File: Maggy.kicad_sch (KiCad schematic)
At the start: 75 parts, among them CN1 0430450800, CN2 430451000, J1 XY308-2.54-2P, J2 XY308-2.54-2P, J3 XY308-2.54-2P, J4 XY308-2.54-2P, U1 CH224K, U10 INA214AIDCKR, U11 Socket for Teensy 4.1 (2x 1x2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, U12 INA214AIDCKR, U13 INA214AIDCKR, U14 TMAG5170A2DGKR, U15 TMAG5170A2DGKR, U16 TMAG5170A2DGKR, U17 TMAG5170A2DGKR, U18 TMAG5170A2DGKR, U2 A4950ELJTR-T, U3 A4950ELJTR-T, U4 A4950ELJTR-T, U5 A4950ELJTR-T, U6 TLV2372, U7 LM1117S-3.3, U8 LM1117S-5.0, U9 INA214AIDCKR

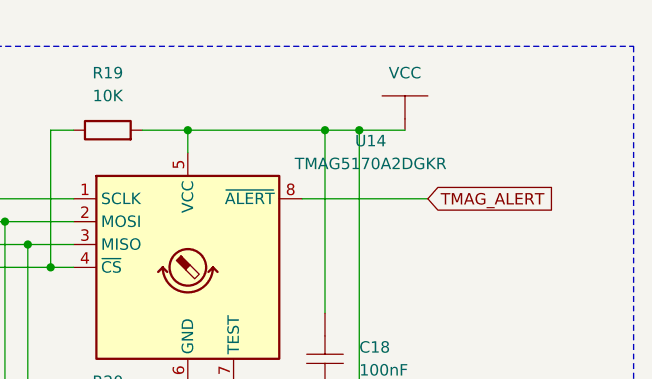
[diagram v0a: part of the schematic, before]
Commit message: fix: update SPI-sensors' power source from VCC to 3v3
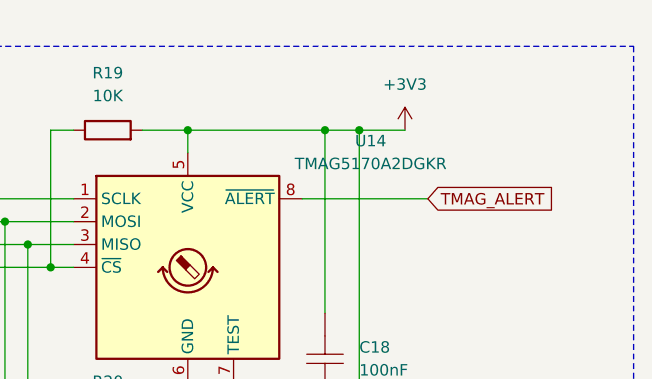
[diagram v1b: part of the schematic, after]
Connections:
- net VCC is gone; now on net +3V3: C18.2, C19.2, C20.2, C21.2, C22.2, R19.2, R20.2, R21.2, R22.2, R23.2, U14.5 (VCC), U15.5 (VCC), U16.5 (VCC), U17.5 (VCC), U18.5 (VCC)
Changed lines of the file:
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@@
 	)
 	(symbol
+		(lib_id "power:+3V3")
+		(at 397.51 31.75 0)
+		(unit 1)
+		(body_style 1)
+		(exclude_from_sim no)
+		(in_bom yes)
+		(on_board yes)
+		(in_pos_files yes)
+		(dnp no)
+		(fields_autoplaced yes)
+		(property "Reference" "#PWR056"
+			(at 397.51 35.56 0)
+			(hide yes)
+			(show_name no)
+			(do_not_autoplace no)
+			(effects
+				(font
+					(size 1.27 1.27)
+				)
+			)
+		)
+		(property "Value" "+3V3"
+			(at 397.51 26.67 0)
+			(show_name no)
+			(do_not_autoplace no)
+			(effects
+				(font
+					(size 1.27 1.27)
+				)
+			)
+		)
+		(property "Footprint" ""
+			(at 397.51 31.75 0)
+			(hide yes)
+			(show_name no)
+			(do_not_autoplace no)
+			(effects
+				(font
+					(size 1.27 1.27)
+				)
+			)
+		)
+		(property "Datasheet" ""
+			(at 397.51 31.75 0)
+			(hide yes)
+			(show_name no)
+			(do_not_autoplace no)
+			(effects
+				(font
+					(size 1.27 1.27)
+				)
+			)
+		)
+		(property "Description" "Power symbol creates a global label with name \"+3V3\""
+			(at 397.51 31.75 0)
+			(hide yes)
+			(show_name no)
+			(do_not_autoplace no)
+			(effects
+				(font
+					(size 1.27 1.27)
+				)
+			)
+		)
+		(pin "1"
+		)
+		(instances
+			(project "Maggy"
+				(path "/52283d6a-1d9f-44e8-81a2-e61315819c23"
+					(reference "#PWR056")
+					(unit 1)
+				)
+			)
+		)
+	)
+	(symbol
 		(lib_id "ProPrj_Mag-easyedapro:CAP")
 		(at 388.62 194.31 270)
@@
 					(unit 1)
 				)
-			)
-		)
-	)
-	(symbol
-		(lib_name "Power-VCC_2")
-		(lib_id "ProPrj_Mag-easyedapro:Power-VCC")
-		(at 397.51 31.75 0)
-		(unit 1)
-		(body_style 1)
-		(exclude_from_sim no)
-		(in_bom yes)
-		(on_board yes)
-		(in_pos_files yes)
-		(dnp no)
-		(fields_autoplaced yes)
-		(property "Reference" "#PWR056"
-			(at 397.51 31.75 0)
-			(hide yes)
-			(show_name no)
-			(do_not_autoplace no)
-			(effects
-				(font
-					(size 1.27 1.27)
-				)
-			)
-		)
-		(property "Value" "VCC"
-			(at 397.51 25.4 0)
-			(show_name no)
-			(do_not_autoplace no)
-			(effects
-				(font
-					(size 1.27 1.27)
-				)
-			)
-		)
-		(property "Footprint" "ProPrj_Mag-easyedapro:"
-			(at 397.51 31.75 0)
-			(hide yes)
-			(show_name no)
-			(do_not_autoplace no)
-			(effects
-				(font
-					(size 1.27 1.27)
-				)
-			)
-		)
-		(property "Datasheet" ""
-			(at 397.51 31.75 0)
-			(hide yes)
-			(show_name no)
-			(do_not_autoplace no)
-			(effects
-				(font
-					(size 1.27 1.27)
-				)
-			)
-		)
-		(property "Description" ""
-			(at 397.51 31.75 0)
-			(hide yes)
-			(show_name no)
-			(do_not_autoplace no)
-			(effects
-				(font
-					(size 1.27 1.27)
-				)
-			)
-		)
-		(pin "1"
-		)
-		(instances
-			(project "Maggy"
-				(path "/52283d6a-1d9f-44e8-81a2-e61315819c23"
-					(reference "#PWR056")
-					(unit 1)
-				)

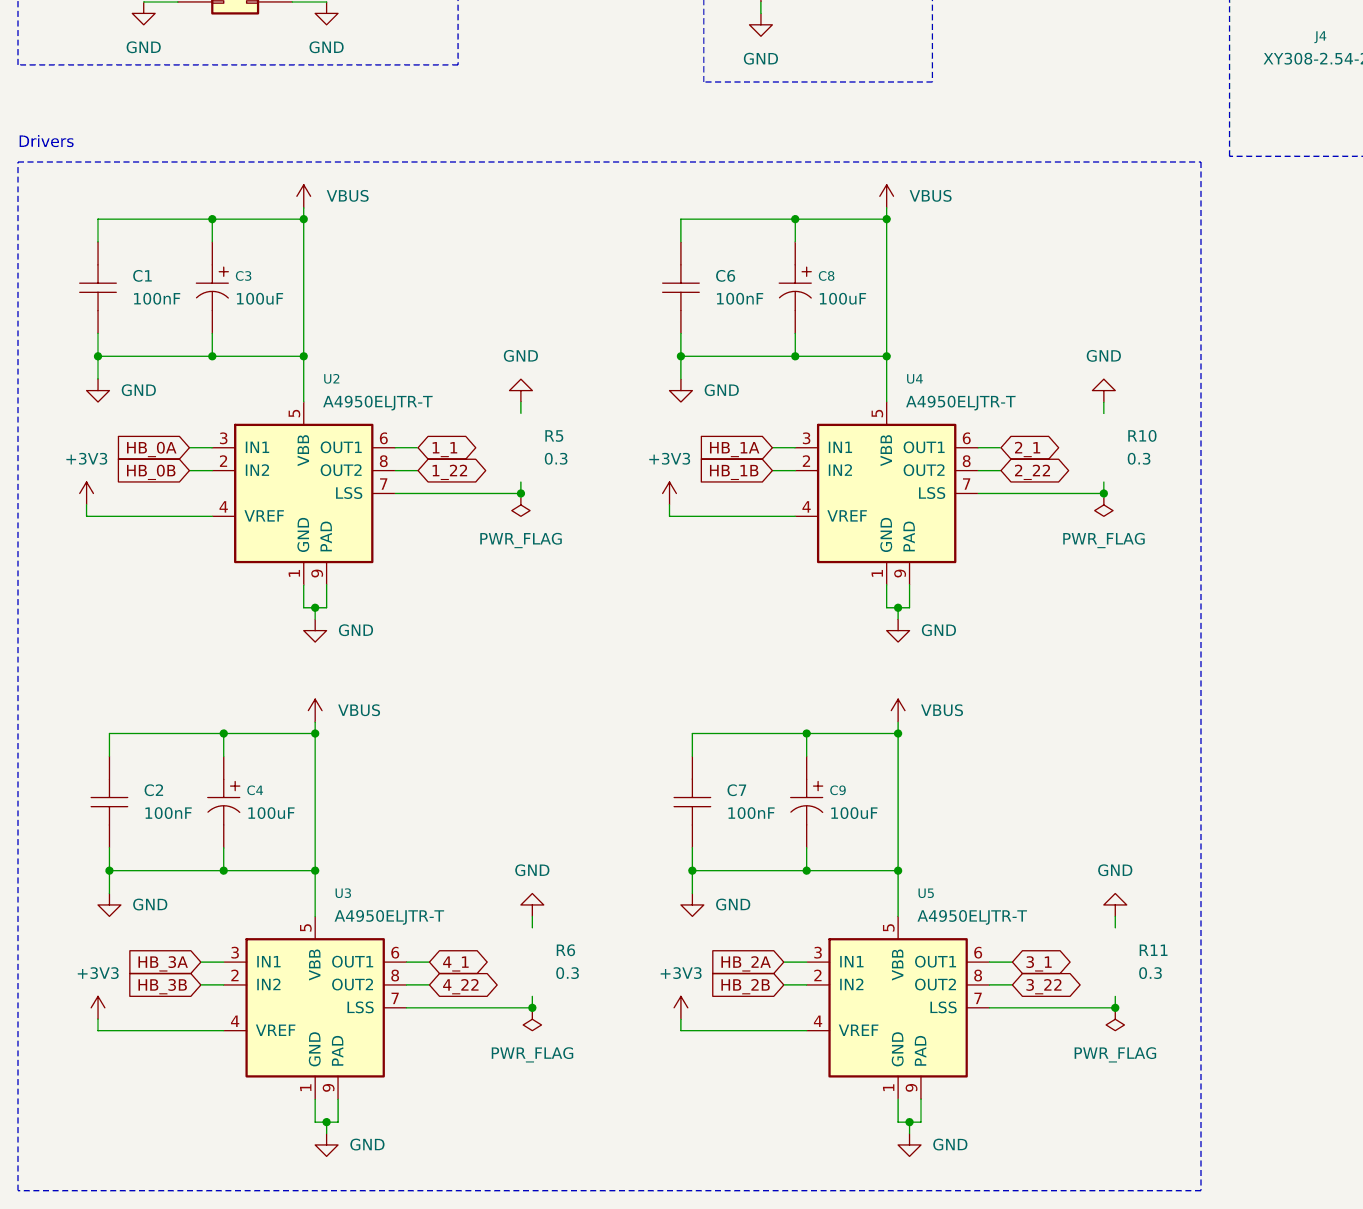
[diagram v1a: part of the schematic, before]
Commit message: fix!: resolve short between VBUS and GND near motor drivers
During the migration from EasyEDA, a mistake was introduced shorting VBUS to GND near the power supply for each motor driver. This was caught by the ERC, and this commit removes the shorted connection.
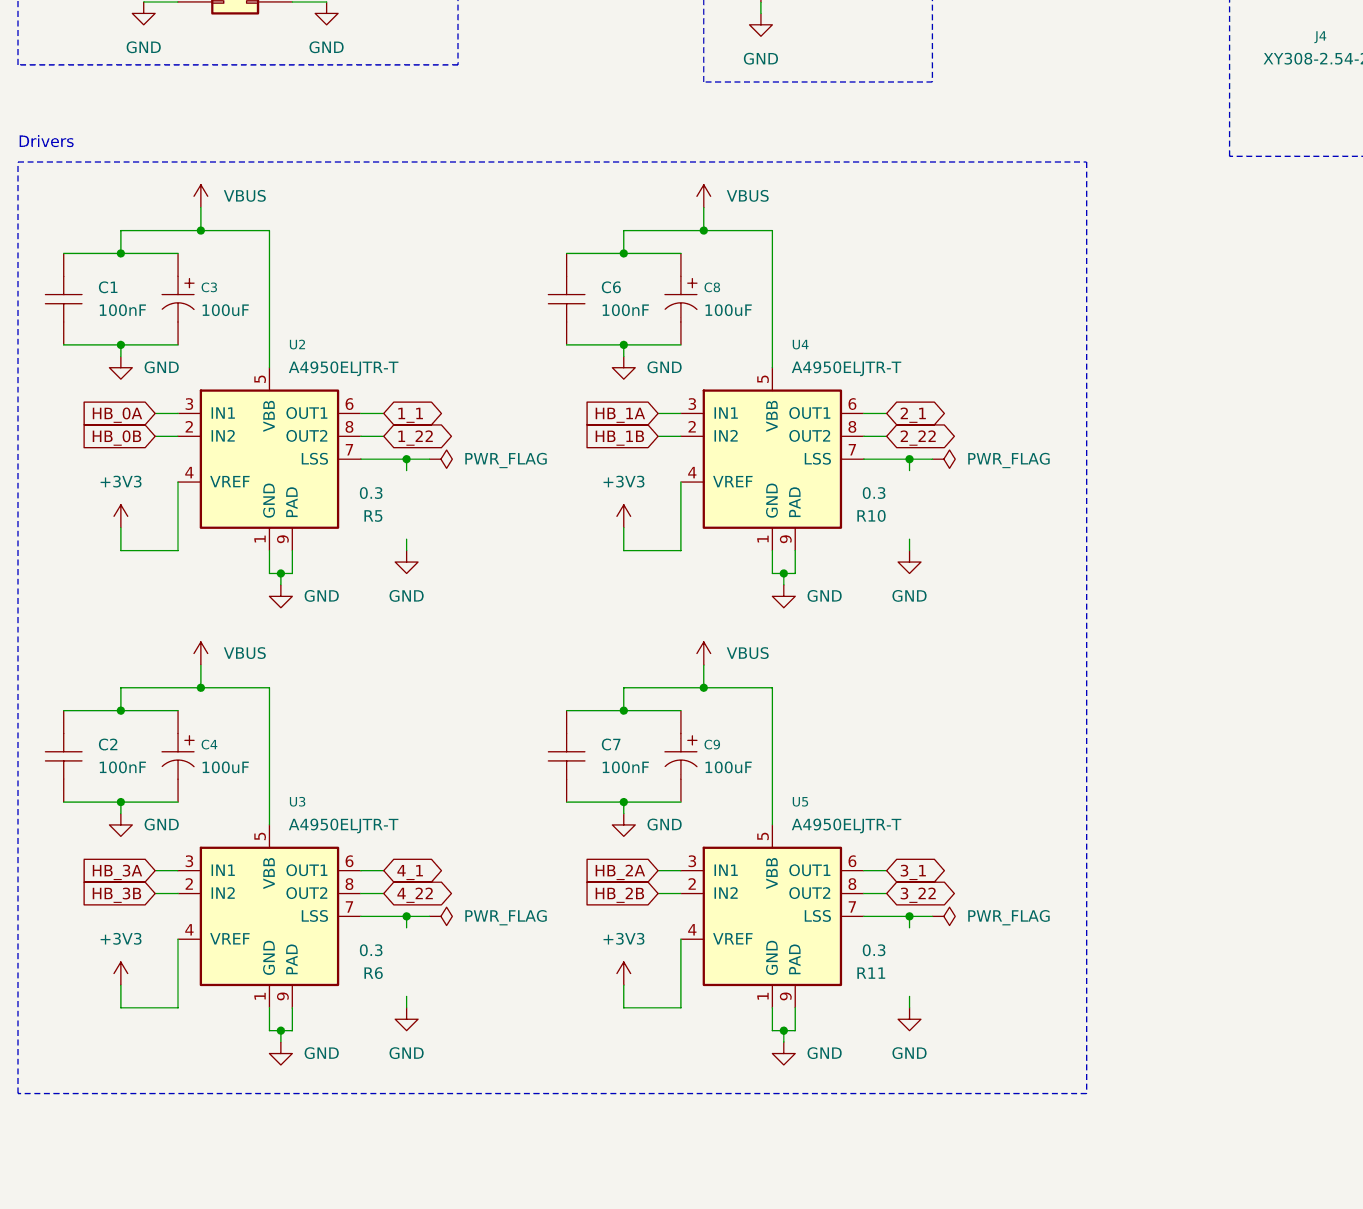
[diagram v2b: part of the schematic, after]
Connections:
- net GND: no longer C1.1, C10.1, C11.1, C2.1, C3.1, C4.1, C6.1, C7.1, C8.1, C9.1, R1.2, R2.2, R7.2, U2.5 (VBB), U3.5 (VBB), U4.5 (VBB), U5.5 (VBB), U7.3 (VI), U8.3 (VI), USBC1.A4 (VBUS), USBC1.A9 (VBUS), USBC1.B4 (VBUS), USBC1.B9 (VBUS)
- new net VBUS: C1.1, C10.1, C11.1, C2.1, C3.1, C4.1, C6.1, C7.1, C8.1, C9.1, R1.2, R2.2, R7.2, U2.5 (VBB), U3.5 (VBB), U4.5 (VBB), U5.5 (VBB), U7.3 (VI), U8.3 (VI), USBC1.A4 (VBUS), USBC1.A9 (VBUS), USBC1.B4 (VBUS), USBC1.B9 (VBUS)
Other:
- moved on the sheet: C1, C3, U2

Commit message: chore: replace all EasyEDA capacitor symbols with KiCad native ones
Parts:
- C1, C10, C11, C12, C13, C14, C15, C16, C17, C18, C19, C2, C20, C21, C22, C5, C6, C7: symbol ProPrj_Mag-easyedapro:CAP -> Device:C
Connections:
- net +3V3: now also C13.2, C14.1, C15.1, C16.1, C17.1, C18.1, C19.1, C20.1, C21.1, C22.1, C5.2; no longer C13.1, C14.2, C15.2, C16.2, C17.2, C18.2, C19.2, C20.2, C21.2, C22.2, C5.1
- net +5V: now also C12.2; no longer C12.1
- net GND: now also C1.1, C10.1, C11.1, C12.1, C13.1, C14.2, C15.2, C16.2, C17.2, C18.2, C19.2, C2.1, C20.2, C21.2, C22.2, C5.1, C6.1, C7.1; no longer C1.2, C10.2, C11.2, C12.2, C13.2, C14.1, C15.1, C16.1, C17.1, C18.1, C19.1, C2.2, C20.1, C21.1, C22.1, C5.2, C6.2, C7.2
- net VBUS: now also C1.2, C10.2, C11.2, C2.2, C6.2, C7.2; no longer C1.1, C10.1, C11.1, C2.1, C6.1, C7.1

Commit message: chore: replace all EasyEDA polarized capacitor symbols with KiCad native ones
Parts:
- C3, C4, C8, C9: symbol ProPrj_Mag-easyedapro:RST100UF35V009 -> Device:C_Polarized_US
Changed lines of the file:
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@@
 	(wire
 		(pts
+			(xy 35.56 209.55) (xy 35.56 210.82)
+		)
+		(stroke
+			(width 0)
+			(type default)
+		)
+	)
+	(wire
+		(pts
 			(xy 29.21 207.01) (xy 29.21 209.55)
 		)
@@
 	(wire
 		(pts
+			(xy 35.56 260.35) (xy 35.56 261.62)
+		)
+		(stroke
+			(width 0)
+			(type default)
+		)
+	)
+	(wire
+		(pts
 			(xy 269.24 280.67) (xy 302.26 280.67)
 		)
@@
 	(wire
 		(pts
+			(xy 91.44 209.55) (xy 91.44 210.82)
+		)
+		(stroke
+			(width 0)
+			(type default)
+		)
+	)
+	(wire
+		(pts
 			(xy 233.68 71.12) (xy 234.95 71.12)
 		)
@@
 	(wire
 		(pts
+			(xy 35.56 218.44) (xy 35.56 219.71)
+		)
+		(stroke
+			(width 0)
+			(type default)
+		)
+	)
+	(wire
+		(pts
 			(xy 88.9 278.13) (xy 91.44 278.13)
 		)
@@
 	(wire
 		(pts
+			(xy 91.44 218.44) (xy 91.44 219.71)
+		)
+		(stroke
+			(width 0)
+			(type default)
+		)
+	)
+	(wire
+		(pts
+			(xy 91.44 260.35) (xy 91.44 261.62)
+		)
+		(stroke
+			(width 0)
+			(type default)
+		)
+	)
+	(wire
+		(pts
 			(xy 396.24 165.1) (xy 396.24 199.39)
 		)
@@
 	(wire
 		(pts
+			(xy 91.44 269.24) (xy 91.44 270.51)
+		)
+		(stroke
+			(width 0)
+			(type default)
+		)
+	)
+	(wire
+		(pts
 			(xy 378.46 199.39) (xy 388.62 199.39)
 		)
@@
 	(wire
 		(pts
+			(xy 35.56 269.24) (xy 35.56 270.51)
+		)
+		(stroke
+			(width 0)
+			(type default)
+		)
+	)
+	(wire
+		(pts
 			(xy 114.3 278.13) (xy 111.76 278.13)
 		)
@@
 	)
 	(symbol
-		(lib_id "ProPrj_Mag-easyedapro:RST100UF35V009")
-		(at 35.56 214.63 270)
+		(lib_id "Device:C_Polarized_US")
+		(at 35.56 214.63 0)
 		(unit 1)
-		(body_style 0)
+		(body_style 1)
 		(exclude_from_sim no)
 		(in_bom yes)
@@
 		(fields_autoplaced yes)
 		(property "Reference" "C3"
-			(at 38.1 213.36 90)
+			(at 39.37 212.725 0)
 			(show_name no)
 			(do_not_autoplace no)
@@
 		)
 		(property "Value" "100uF"
-			(at 38.1 215.8999 90)
+			(at 39.37 215.2649 0)
 			(show_name no)
 			(do_not_autoplace no)
@@
 			)
 		)
-		(property "Description" "Capacitance: Tolerance:±20% Tolerance:±20% Rated Voltage: Ripple Current:84mA@120Hz Equivalent Series Resistance(ESR):- φD: L: Lifetime @ Temp:2000hrs@105℃ Operating Temperature:-40℃~+105℃ Operating Temperature:-40℃~+105℃"
-			(at 35.56 214.63 90)
+		(property "Description" "Polarized capacitor, US symbol"
+			(at 35.56 214.63 0)
 			(hide yes)
 			(show_name no)
@@
 					(size 1.27 1.27)
 				)
-				(justify left bottom)
 			)
 		)
@@
 	)
 	(symbol
-		(lib_id "ProPrj_Mag-easyedapro:RST100UF35V009")
-		(at 35.56 265.43 270)
+		(lib_id "Device:C_Polarized_US")
+		(at 35.56 265.43 0)
 		(unit 1)
 		(body_style 0)
@@
 		(fields_autoplaced yes)
 		(property "Reference" "C4"
-			(at 38.1 264.16 90)
+			(at 39.37 263.525 0)
 			(show_name no)
 			(do_not_autoplace no)
@@
 		)
 		(property "Value" "100uF"
-			(at 38.1 266.6999 90)
+			(at 39.37 266.0649 0)
 			(show_name no)
 			(do_not_autoplace no)
@@
 			)
 		)
-		(property "Description" "Capacitance: Tolerance:±20% Tolerance:±20% Rated Voltage: Ripple Current:84mA@120Hz Equivalent Series Resistance(ESR):- φD: L: Lifetime @ Temp:2000hrs@105℃ Operating Temperature:-40℃~+105℃ Operating Temperature:-40℃~+105℃"
-			(at 35.56 265.43 90)
+		(property "Description" "Polarized capacitor, US symbol"
+			(at 35.56 265.43 0)
 			(hide yes)
 			(show_name no)
@@
 					(size 1.27 1.27)
 				)
-				(justify left bottom)
 			)
 		)
@@
 	)
 	(symbol
-		(lib_id "ProPrj_Mag-easyedapro:RST100UF35V009")
-		(at 91.44 265.43 270)
+		(lib_id "Device:C_Polarized_US")
+		(at 91.44 265.43 0)
 		(unit 1)
 		(body_style 0)
@@
 		(fields_autoplaced yes)
 		(property "Reference" "C9"
-			(at 93.98 264.16 90)
+			(at 95.25 263.525 0)
 			(show_name no)
 			(do_not_autoplace no)
@@
 		)
 		(property "Value" "100uF"
-			(at 93.98 266.6999 90)
+			(at 95.25 266.0649 0)
 			(show_name no)
 			(do_not_autoplace no)
@@
 			)
 		)
-		(property "Description" "Capacitance: Tolerance:±20% Tolerance:±20% Rated Voltage: Ripple Current:84mA@120Hz Equivalent Series Resistance(ESR):- φD: L: Lifetime @ Temp:2000hrs@105℃ Operating Temperature:-40℃~+105℃ Operating Temperature:-40℃~+105℃"
-			(at 91.44 265.43 90)
+		(property "Description" "Polarized capacitor, US symbol"
+			(at 91.44 265.43 0)
 			(hide yes)
 			(show_name no)
@@
 					(size 1.27 1.27)
 				)
-				(justify left bottom)
 			)
 		)
@@
 	)
 	(symbol
-		(lib_id "ProPrj_Mag-easyedapro:RST100UF35V009")
-		(at 91.44 214.63 270)
+		(lib_id "Device:C_Polarized_US")
+		(at 91.44 214.63 0)
 		(unit 1)
 		(body_style 0)
@@
 		(fields_autoplaced yes)
 		(property "Reference" "C8"
-			(at 93.98 213.36 90)
+			(at 95.25 212.725 0)
 			(show_name no)
 			(do_not_autoplace no)
@@
 		)
 		(property "Value" "100uF"
-			(at 93.98 215.8999 90)
+			(at 95.25 215.2649 0)
 			(show_name no)
 			(do_not_autoplace no)
@@
 			)
 		)
-		(property "Description" "Capacitance: Tolerance:±20% Tolerance:±20% Rated Voltage: Ripple Current:84mA@120Hz Equivalent Series Resistance(ESR):- φD: L: Lifetime @ Temp:2000hrs@105℃ Operating Temperature:-40℃~+105℃ Operating Temperature:-40℃~+105℃"
-			(at 91.44 214.63 90)
+		(property "Description" "Polarized capacitor, US symbol"
+			(at 91.44 214.63 0)
 			(hide yes)
 			(show_name no)
@@
 					(size 1.27 1.27)
 				)
-				(justify left bottom)
 			)
 		)

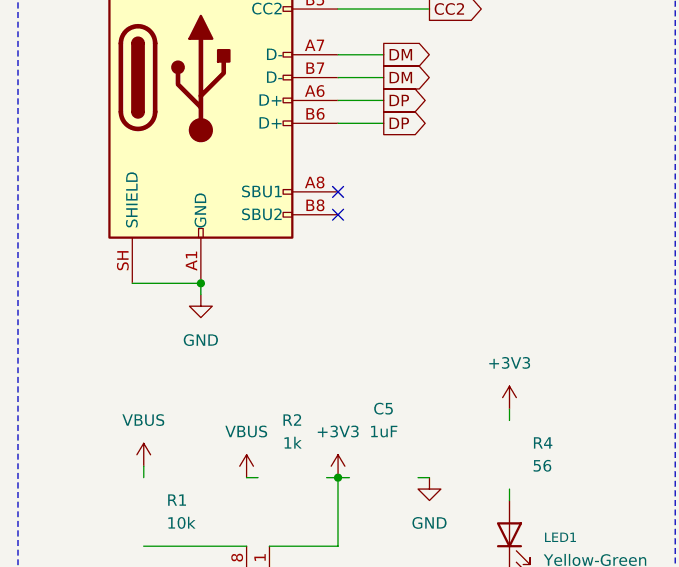
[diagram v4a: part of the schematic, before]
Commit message: chore: add power flag to USB-C GND connection
This indicates to KiCad that the external, incoming GND connection is driven, preventing ERC warnings and errors about "Power inputs" not being connected to any "Power outputs", etc.
Especially annoying when wiring decoupling capacitors
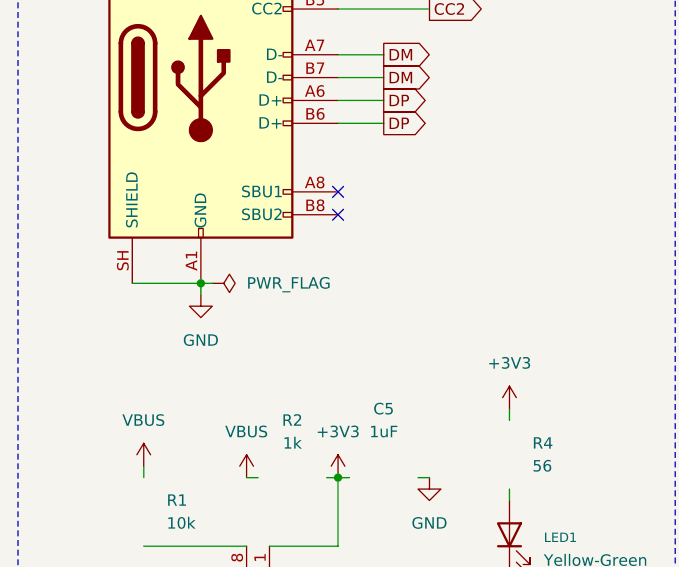
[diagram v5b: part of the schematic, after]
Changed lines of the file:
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@@
 	(wire
 		(pts
+			(xy 38.1 72.39) (xy 39.37 72.39)
+		)
+		(stroke
+			(width 0)
+			(type default)
+		)
+	)
+	(wire
+		(pts
 			(xy 392.43 100.33) (xy 392.43 134.62)
 		)
@@
 					(unit 1)
 				)
+			)
+		)
+	)
+	(symbol
+		(lib_id "power:PWR_FLAG")
+		(at 39.37 72.39 270)
+		(unit 1)
+		(body_style 1)
+		(exclude_from_sim no)
+		(in_bom yes)
+		(on_board yes)
+		(in_pos_files yes)
+		(dnp no)
+		(fields_autoplaced yes)
+		(property "Reference" "#FLG06"
+			(at 41.275 72.39 0)
+			(hide yes)
+			(show_name no)
+			(do_not_autoplace no)
+			(effects
+				(font
+					(size 1.27 1.27)
+				)
+			)
+		)
+		(property "Value" "PWR_FLAG"
+			(at 43.18 72.3899 90)
+			(show_name no)
+			(do_not_autoplace no)
+			(effects
+				(font
+					(size 1.27 1.27)
+				)
+				(justify left)
+			)
+		)
+		(property "Footprint" ""
+			(at 39.37 72.39 0)
+			(hide yes)
+			(show_name no)
+			(do_not_autoplace no)
+			(effects
+				(font
+					(size 1.27 1.27)
+				)
+			)
+		)
+		(property "Datasheet" ""
+			(at 39.37 72.39 0)
+			(hide yes)
+			(show_name no)
+			(do_not_autoplace no)
+			(effects
+				(font
+					(size 1.27 1.27)
+				)
+			)
+		)
+		(property "Description" "Special symbol for telling ERC where power comes from"
+			(at 39.37 72.39 0)
+			(hide yes)
+			(show_name no)
+			(do_not_autoplace no)
+			(effects
+				(font
+					(size 1.27 1.27)
+				)
+			)
+		)
+		(pin "1"
+		)
+		(instances
+			(project "Maggy"
+				(path "/52283d6a-1d9f-44e8-81a2-e61315819c23"
+					(reference "#FLG06")
+					(unit 1)
+				)

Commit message: chore: update footprints for solenoid terminal blocks
They were referencing a non-existing footprint lost during the EasyEDA import, updated to a KiCad native one
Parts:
- J1, J2, J3, J4: footprint ProPrj_Maggy 4.1_2025-02-07-import-fps:CONN-TH_XY308-2.54-2P -> TerminalBlock:TerminalBlock_Xinya_XY308-2.54-2P_1x02_P2.54mm_Horizontal
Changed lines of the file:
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@@
 			)
 		)
-		(property "Footprint" "ProPrj_Maggy 4.1_2025-02-07-import-fps:CONN-TH_XY308-2.54-2P"
+		(property "Footprint" "TerminalBlock:TerminalBlock_Xinya_XY308-2.54-2P_1x02_P2.54mm_Horizontal"
 			(at 162.56 166.37 0)
 			(hide yes)
@@
 			)
 		)
-		(property "Footprint" "ProPrj_Maggy 4.1_2025-02-07-import-fps:CONN-TH_XY308-2.54-2P"
+		(property "Footprint" "TerminalBlock:TerminalBlock_Xinya_XY308-2.54-2P_1x02_P2.54mm_Horizontal"
 			(at 162.56 191.77 0)
 			(hide yes)
@@
 			)
 		)
-		(property "Footprint" "ProPrj_Maggy 4.1_2025-02-07-import-fps:CONN-TH_XY308-2.54-2P"
+		(property "Footprint" "TerminalBlock:TerminalBlock_Xinya_XY308-2.54-2P_1x02_P2.54mm_Horizontal"
 			(at 162.56 179.07 0)
 			(hide yes)
@@
 			)
 		)
-		(property "Footprint" "ProPrj_Maggy 4.1_2025-02-07-import-fps:CONN-TH_XY308-2.54-2P"
+		(property "Footprint" "TerminalBlock:TerminalBlock_Xinya_XY308-2.54-2P_1x02_P2.54mm_Horizontal"
 			(at 162.56 153.67 0)
 			(hide yes)
